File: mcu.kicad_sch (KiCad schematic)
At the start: 23 parts, among them J6 Conn_TempMotor, SW4 SW_Reset, U5 STM32F103RETx, Y1 ABM3B-16MHz

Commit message: Rename files Remove unnecessary contents
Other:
- removed sheet EndstopLeft
- removed sheet ExternalEncoder
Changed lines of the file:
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@@
-    (stroke (width 0) (type default) (color 0 0 0 0))
-  )
-  (wire (pts (xy 35.56 31.75) (xy 34.29 31.75))
     (stroke (width 0) (type default) (color 0 0 0 0))
   )
@@
     (stroke (width 0) (type default) (color 0 0 0 0))
   )
-  (wire (pts (xy 35.56 20.32) (xy 34.29 20.32))
-    (stroke (width 0) (type default) (color 0 0 0 0))
-  )
   (wire (pts (xy 273.05 124.46) (xy 275.59 124.46))
     (stroke (width 0) (type default) (color 0 0 0 0))
@@
   )
   (polyline (pts (xy 259.08 50.8) (xy 283.21 50.8))
-    (stroke (width 0) (type default) (color 0 0 0 0))
-  )
-  (wire (pts (xy 34.29 17.78) (xy 35.56 17.78))
     (stroke (width 0) (type default) (color 0 0 0 0))
   )
@@
     (effects (font (size 1.27 1.27)) (justify left bottom))
   )
-  (label "I2C2_SCL" (at 35.56 20.32 0)
-    (effects (font (size 1.27 1.27)) (justify left bottom))
-  )
   (label "I2C1_SDA" (at 180.34 102.87 0)
-    (effects (font (size 1.27 1.27)) (justify left bottom))
-  )
-  (label "I2C2_SDA" (at 35.56 17.78 0)
     (effects (font (size 1.27 1.27)) (justify left bottom))
   )
@@
   (label "~{RST}" (at 111.76 41.91 180)
     (effects (font (size 1.27 1.27)) (justify right bottom))
-  )
-  (label "endstopRight" (at 35.56 31.75 0)
-    (effects (font (size 1.27 1.27)) (justify left bottom))
   )
   (label "SWDIO" (at 269.24 64.77 180)
@@
     (pin "1")
   )
-  (sheet (at 13.97 15.24) (size 20.32 7.62) (fields_autoplaced)
-    (stroke (width 0) (type solid) (color 0 0 0 0))
-    (fill (color 0 0 0 0.0000))
-    (property "Sheet name" "ExternalEncoder" (id 0) (at 13.97 14.5284 0)
-      (effects (font (size 1.27 1.27)) (justify left bottom))
-    )
-    (property "Sheet file" "ExternalEncoder.kicad_sch" (id 1) (at 13.97 23.4446 0)
-      (effects (font (size 1.27 1.27)) (justify left top))
-    )
-    (pin "SDA" bidirectional (at 34.29 17.78 0)
-      (effects (font (size 1.27 1.27)) (justify right))
-    )
-    (pin "SCL" input (at 34.29 20.32 0)
-      (effects (font (size 1.27 1.27)) (justify right))
-    )
-  )
-  (sheet (at 13.97 29.21) (size 20.32 5.08) (fields_autoplaced)
-    (stroke (width 0) (type solid) (color 0 0 0 0))
-    (fill (color 0 0 0 0.0000))
-    (property "Sheet name" "EndstopLeft" (id 0) (at 13.97 28.4984 0)
-      (effects (font (size 1.27 1.27)) (justify left bottom))
-    )
-    (property "Sheet file" "OpticalEndstop.kicad_sch" (id 1) (at 13.97 34.8746 0)
-      (effects (font (size 1.27 1.27)) (justify left top))
-    )
-    (pin "Switch" output (at 34.29 31.75 0)
-      (effects (font (size 1.27 1.27)) (justify right))
-    )
-  )
   (sheet (at 16.51 147.32) (size 20.32 7.62) (fields_autoplaced)

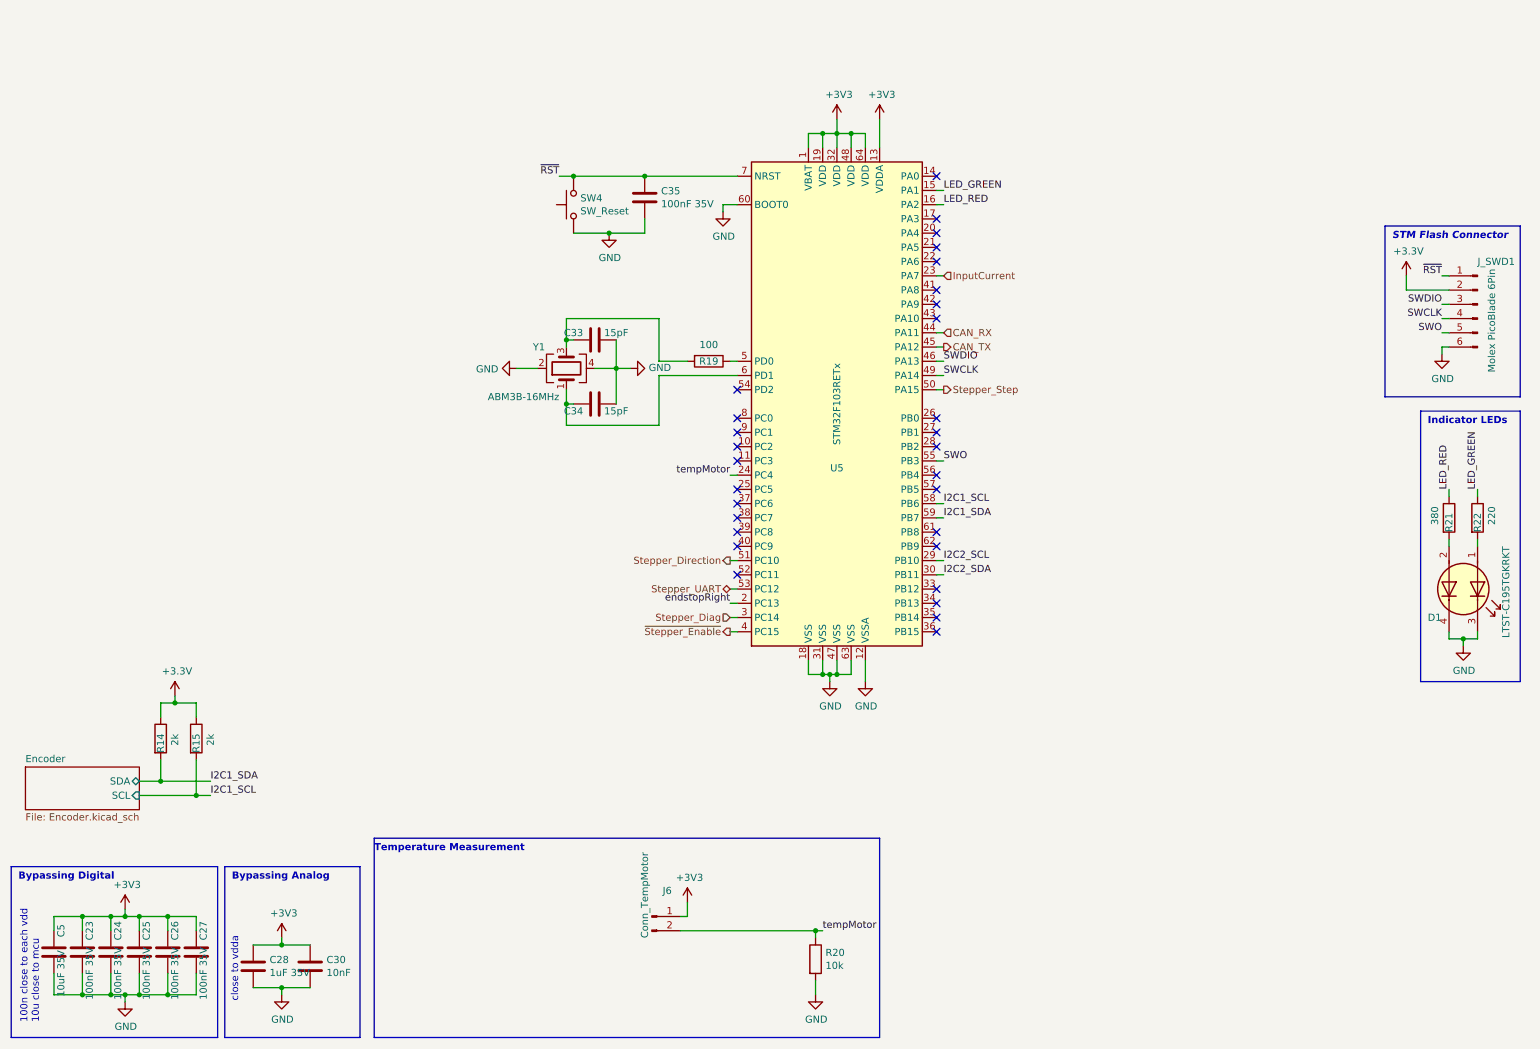
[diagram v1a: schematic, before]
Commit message: Rearrange schematic and some cleanups Add 5V buck converter Update values for TMC2209 Add EEPROM Switch to STM32G0B1KE
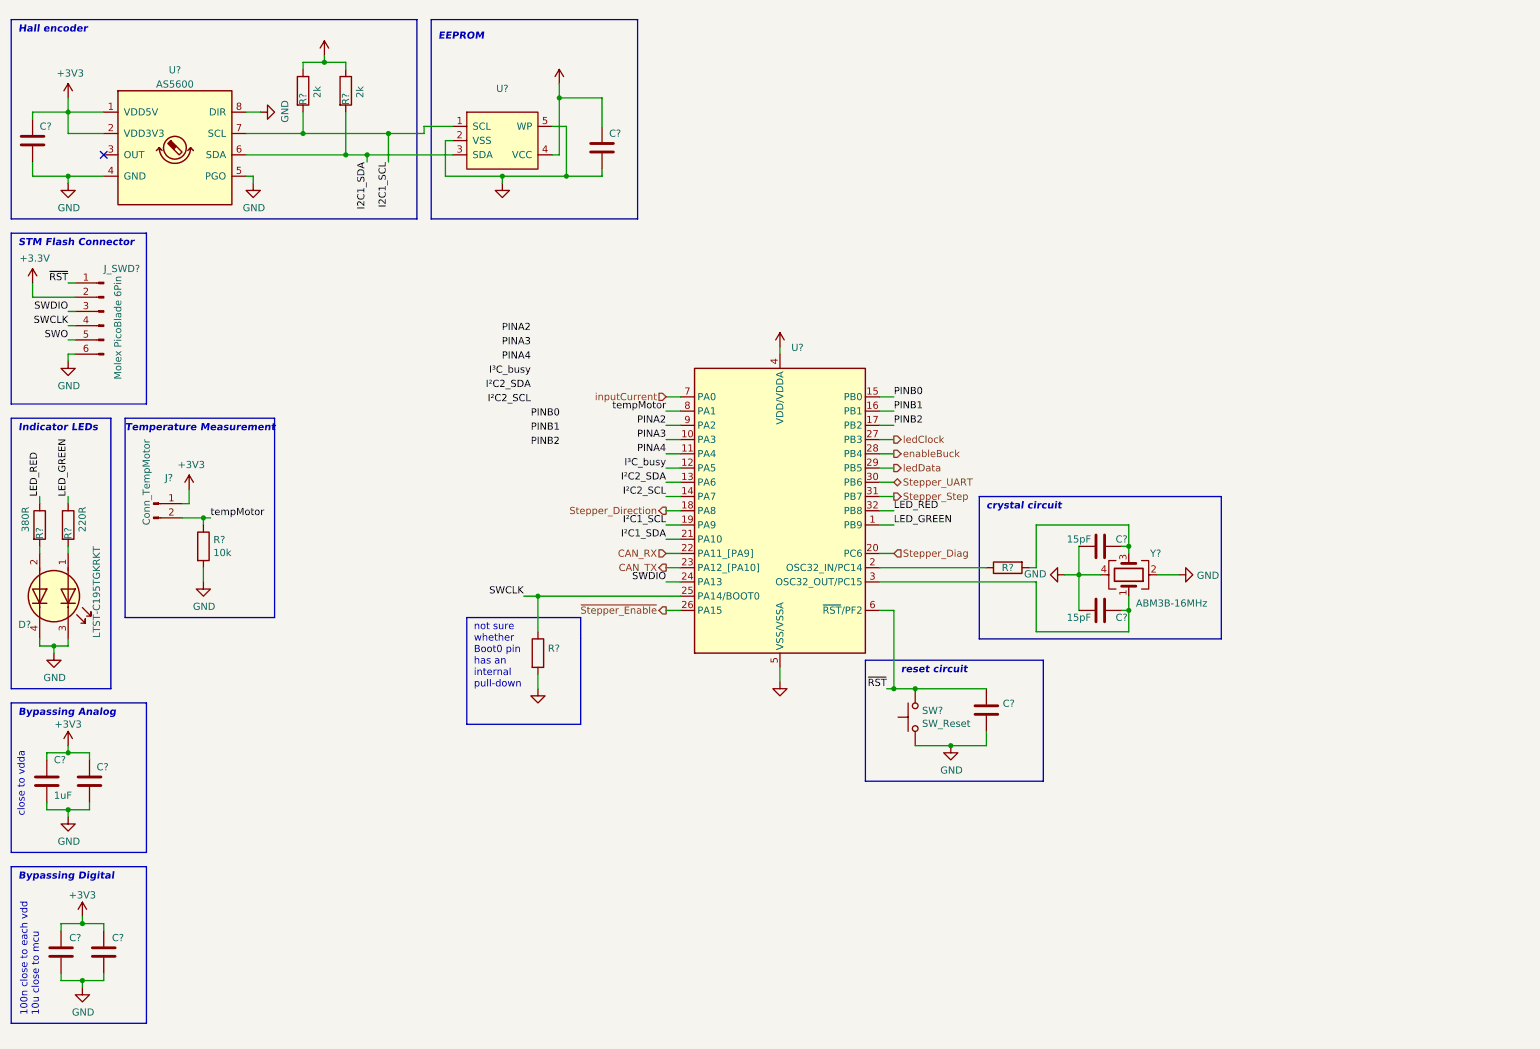
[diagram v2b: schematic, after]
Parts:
- removed C24, C25, C26, C27: 100nF 35V, Capacitor_SMD:C_0603_1608Metric, symbol Device:C
- removed D1: LTST-C195TGKRKT, standardContent:LED_LiteOn_LTST-C195TGKRKT, symbol Device:LED_Dual_AACC
- removed U5: STM32F103RETx, Package_QFP:LQFP-64_10x10mm_P0.5mm, symbol MCU_ST_STM32F1:STM32F103RETx
- added C?: (no value), symbol Device:C
- added C?: ~, Capacitor_SMD:C_0603_1608Metric, symbol Device:C
- added D?: LTST-C195TGKRKT, extraFootprints:LED_LiteOn_LTST-C195TGKRKT, symbol Device:LED_Dual_AAKK
- added R?: (no value), symbol Device:R
- added U?: (no value), Package_TO_SOT_SMD:SOT-23-5, symbol extraSymbols:24LC64
- added U?: (no value), symbol MCU_ST_STM32G0:STM32G071KxT
- added U?: AS5600, symbol extraSymbols:AS5600
- C?: renamed from C35; value 100nF 35V -> (none)
- C?: renamed from C23; value 100nF 35V -> (none)
- C?: renamed from C28; value 1uF 35V -> 1uF
- C?: renamed from C30; value 10nF -> (none)
- C?: renamed from C5; value 10uF 35V -> (none)
- R?: renamed from R19; value 100 -> (none)
- R?: renamed from R21; value 380 -> 380R
- R?: renamed from R22; value 220 -> 220R
- SW?: renamed from SW4; footprint standardContent:SW_SPST_PTS636_SM25F -> extraFootprints:PTS636_F-leads
- renumbered C33 to C?, C34 to C?, J6 to J?, J_SWD1 to J_SWD?, R20 to R?, R15 to R?, R14 to R?, Y1 to Y?
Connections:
- net +3V3: now also C?.1, C?.1, U?.1 (VDD5V), U?.2 (VDD3V3), U?.4 (VCC), U?.4 (VDD/VDDA)
- net CAN_RX: now also U?.22 (PA11_[PA9])
- net CAN_TX: now also U?.23 (PA12_[PA10])
- net GND: now also C?.2, C?.2, D?.3 (K1), D?.4 (K2), R?.2, U?.2 (VSS), U?.4 (GND), U?.5 (PGO), U?.5 (VSS/VSSA), U?.5 (WP), U?.8 (DIR)
- net I2C1_SCL: now also R?.2, U?.1 (SCL), U?.7 (SCL); no longer R?.2
- net I2C1_SDA: now also R?.2, U?.3 (SDA), U?.6 (SDA); no longer R?.2
- net LED_GREEN: now also U?.1 (PB9)
- net LED_RED: now also U?.32 (PB8)
- net SWCLK: now also R?.1, U?.25 (PA14/BOOT0)
- net SWDIO: now also U?.24 (PA13)
- net Stepper_Diag: now also U?.20 (PC6)
- net Stepper_Direction: now also U?.18 (PA8)
- net Stepper_Step: now also U?.31 (PB7)
- net Stepper_UART: now also U?.30 (PB6)
- net tempMotor: now also U?.8 (PA1)
- net ~{RST}: now also U?.6 (~{RST}/PF2)
- net ~{Stepper_Enable}: now also U?.26 (PA15)
- net at R?.1: now also U?.2 (OSC32_IN/PC14)
- net at C?.2, Y?.1: now also U?.3 (OSC32_OUT/PC15)
- net at R?.2: now also D?.2 (A2)
- net at R?.2: now also D?.1 (A1)
- new net I²C1_SCL: U?.19 (PA9)
- new net I²C1_SDA: U?.21 (PA10)
- new net I²C2_SCL: U?.14 (PA7)
- new net I²C2_SDA: U?.13 (PA6)
- new net I³C_busy: U?.12 (PA5)
- new net PINA2: U?.9 (PA2)
- new net PINA3: U?.10 (PA3)
- new net PINA4: U?.11 (PA4)
- new net PINB0: U?.15 (PB0)
- new net PINB1: U?.16 (PB1)
- new net PINB2: U?.17 (PB2)
- new net enableBuck: U?.28 (PB4)
- new net inputCurrent: U?.7 (PA0)
- new net ledClock: U?.27 (PB3)
- new net ledData: U?.29 (PB5)
- no-connect marks 30 -> 1
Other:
- removed sheet Encoder
- note added: "EEPROM"
- note added: "Hall encoder"
- note added: "crystal circuit"
- note added: "not sure whether Boot0 pin has an internal pull-down"
- note added: "reset circuit"
- moved on the sheet: C?, J?, J_SWD?, R?, SW?, Y?

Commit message: Small changes
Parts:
- C? (x3): value (none) -> 100nF
- C?: value (none) -> 10uF
- C?: value (none) -> 100n
- C?: value ~ -> (none); footprint Capacitor_SMD:C_0603_1608Metric -> (none)
- R?: value (none) -> 100R
- R?: value (none) -> 100k
- U?: value (none) -> 24LC64
- U?: value (none) -> STM32G0B1KET; footprint (none) -> Package_QFP:LQFP-32_7x7mm_P0.8mm
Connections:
- net SWO: no longer names the net of J_SWD?.5 (Pin_5)
- no-connect marks 1 -> 2
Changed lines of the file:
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@@
   (junction (at 48.26 102.87) (diameter 0) (color 0 0 0 0)
   )
+  (no_connect (at 25.4 71.12))
   (no_connect (at 30.48 38.1))
   (wire (pts (xy 213.36 123.19) (xy 196.85 123.19))
@@
   )
   (polyline (pts (xy 13.97 165.1) (xy 13.97 193.04))
-    (stroke (width 0) (type default) (color 0 0 0 0))
-  )
-  (wire (pts (xy 25.4 71.12) (xy 24.13 71.12))
     (stroke (width 0) (type default) (color 0 0 0 0))
   )
@@
     (effects (font (size 1.27 1.27) (thickness 0.254) bold italic) (justify left bottom))
   )
-  (label "SWO" (at 24.13 71.12 180)
-    (effects (font (size 1.27 1.27)) (justify right bottom))
-  )
   (label "LED_RED" (at 171.45 101.6 0)
     (effects (font (size 1.27 1.27)) (justify left bottom))
@@
     (in_bom yes) (on_board yes)
     (property "Reference" "R?" (id 0) (at 191.77 111.76 90))
-    (property "Value" "" (id 1) (at 191.77 108.8136 90))
+    (property "Value" "100R" (id 1) (at 191.77 108.8136 90))
     (property "Footprint" "Resistor_SMD:R_0603_1608Metric" (id 2) (at 191.77 109.982 90)
       (effects (font (size 1.27 1.27)) hide)
@@
       (effects (font (size 1.27 1.27)) (justify left))
     )
-    (property "Value" "" (id 1) (at 190.881 138.303 0)
+    (property "Value" "100nF" (id 1) (at 190.881 138.303 0)
       (effects (font (size 1.27 1.27)) (justify left))
     )
@@
     (in_bom yes) (on_board yes)
     (property "Reference" "C?" (id 0) (at 33.02 177.8 0))
-    (property "Value" "" (id 1) (at 34.29 182.88 0))
+    (property "Value" "100nF" (id 1) (at 34.29 182.88 0))
     (property "Footprint" "Capacitor_SMD:C_0603_1608Metric" (id 2) (at 29.5148 176.53 0)
       (effects (font (size 1.27 1.27)) hide)
@@
       (effects (font (size 1.27 1.27)) (justify left))
     )
-    (property "Value" "" (id 1) (at 29.21 152.4 0)
+    (property "Value" "100nF" (id 1) (at 29.21 152.4 0)
       (effects (font (size 1.27 1.27)) (justify left))
     )
@@
     (in_bom yes) (on_board yes)
     (property "Reference" "C?" (id 0) (at 25.4 177.8 0))
-    (property "Value" "" (id 1) (at 26.67 182.88 0))
+    (property "Value" "10uF" (id 1) (at 26.67 182.88 0))
     (property "Footprint" "Capacitor_SMD:C_1206_3216Metric" (id 2) (at 21.8948 176.53 0)
       (effects (font (size 1.27 1.27)) hide)
@@
     (in_bom yes) (on_board yes)
     (property "Reference" "U?" (id 0) (at 101.6 26.289 0))
-    (property "Value" "" (id 1) (at 101.6 28.6004 0))
+    (property "Value" "24LC64" (id 1) (at 101.6 28.6004 0))
     (property "Footprint" "Package_TO_SOT_SMD:SOT-23-5" (id 2) (at 101.6 36.83 0)
       (effects (font (size 1.27 1.27)) hide)
@@
       (effects (font (size 1.27 1.27)) hide)
     )
-    (property "Value" "" (id 1) (at 151.13 68.8142 0))
+    (property "Value" "+3V3" (id 1) (at 151.13 68.8142 0))
     (property "Footprint" "" (id 2) (at 151.13 72.39 0)
       (effects (font (size 1.27 1.27)) hide)
@@
       (effects (font (size 1.27 1.27)) hide)
     )
-    (property "Value" "" (id 1) (at 111.76 21.8242 0))
+    (property "Value" "+3V3" (id 1) (at 111.76 21.8242 0))
     (property "Footprint" "" (id 2) (at 111.76 25.4 0)
       (effects (font (size 1.27 1.27)) hide)
@@
       (effects (font (size 1.27 1.27)) hide)
     )
-    (property "Value" "" (id 1) (at 107.95 137.7934 0))
+    (property "Value" "GND" (id 1) (at 107.95 137.7934 0))
     (property "Footprint" "" (id 2) (at 107.95 133.35 0)
       (effects (font (size 1.27 1.27)) hide)
@@
       (effects (font (size 1.27 1.27)) hide)
     )
-    (property "Value" "" (id 1) (at 151.13 136.5234 0))
+    (property "Value" "GND" (id 1) (at 151.13 136.5234 0))
     (property "Footprint" "" (id 2) (at 151.13 132.08 0)
       (effects (font (size 1.27 1.27)) hide)
@@
       (effects (font (size 1.27 1.27)) (justify left))
     )
-    (property "Value" "" (id 1) (at 153.1494 75.0371 0)
-      (effects (font (size 1.27 1.27)) (justify left))
-    )
-    (property "Footprint" "" (id 2) (at 148.59 128.27 0)
+    (property "Value" "STM32G0B1KET" (id 1) (at 153.1494 75.0371 0)
+      (effects (font (size 1.27 1.27)) (justify left))
+    )
+    (property "Footprint" "Package_QFP:LQFP-32_7x7mm_P0.8mm" (id 2) (at 148.59 128.27 0)
       (effects (font (size 1.27 1.27)) (justify right) hide)
     )
@@
       (effects (font (size 1.27 1.27)) hide)
     )
-    (property "Value" "" (id 1) (at 69.85 16.7442 0))
+    (property "Value" "+3V3" (id 1) (at 69.85 16.7442 0))
     (property "Footprint" "" (id 2) (at 69.85 20.32 0)
       (effects (font (size 1.27 1.27)) hide)
@@
       (effects (font (size 1.27 1.27)) (justify left))
     )
-    (property "Value" "" (id 1) (at 120.65 39.37 0)
+    (property "Value" "100n" (id 1) (at 120.65 39.37 0)
       (effects (font (size 1.27 1.27)) (justify left))
     )
@@
       (effects (font (size 1.27 1.27)) (justify left))
     )
-    (property "Value" "~" (id 1) (at 12.7 38.1 0)
-      (effects (font (size 1.27 1.27)) (justify left))
-    )
-    (property "Footprint" "Capacitor_SMD:C_0603_1608Metric" (id 2) (at 18.7452 39.37 0)
+    (property "Value" "" (id 1) (at 19.05 38.1 0)
+      (effects (font (size 1.27 1.27)) (justify left))
+    )
+    (property "Footprint" "" (id 2) (at 18.7452 39.37 0)
       (effects (font (size 1.27 1.27)) hide)
     )
@@
       (effects (font (size 1.27 1.27)) hide)
     )
-    (property "Value" "" (id 1) (at 101.6 47.6234 0))
+    (property "Value" "GND" (id 1) (at 101.6 47.6234 0))
     (property "Footprint" "" (id 2) (at 101.6 43.18 0)
       (effects (font (size 1.27 1.27)) hide)
@@
       (effects (font (size 1.27 1.27)) (justify left))
     )
-    (property "Value" "" (id 1) (at 109.728 128.7022 0)
-      (effects (font (size 1.27 1.27)) (justify left))
-    )
+    (property "Value" "100k" (id 1) (at 109.728 128.7022 0)
+      (effects (font (size 1.27 1.27)) (justify left))
+    )
